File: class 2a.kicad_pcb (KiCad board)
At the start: 2 copper layers, 51.3 x 47.5 mm, 36 parts, among them J1 USB_C_Receptacle, J2 Conn_01x02_Pin, J3 Conn_ARM_JTAG_SWD_10, SW1 SW_SPST, U1 STM32G030F6P6, U2 LR4054, U3 TPS613222ADBV, U4 AMS1117-3.3

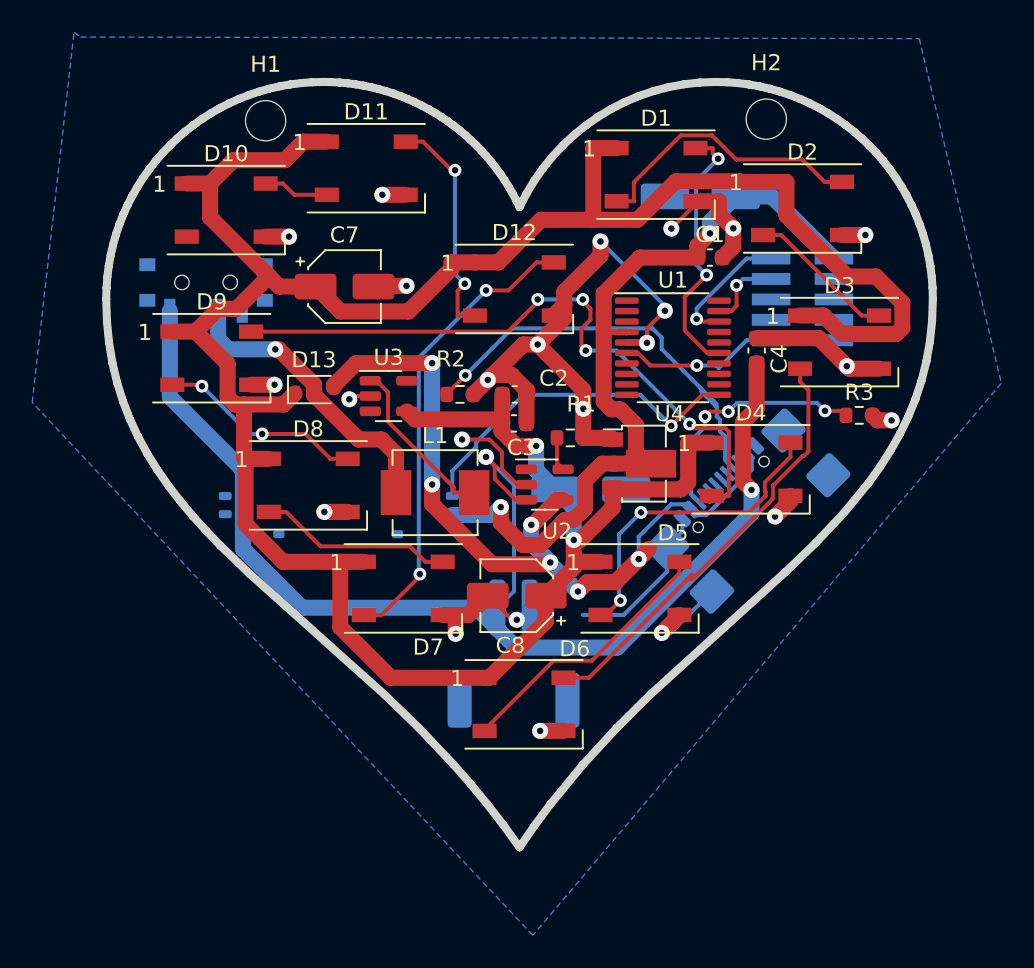
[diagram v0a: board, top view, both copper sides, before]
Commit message: fix resistors for usb-c
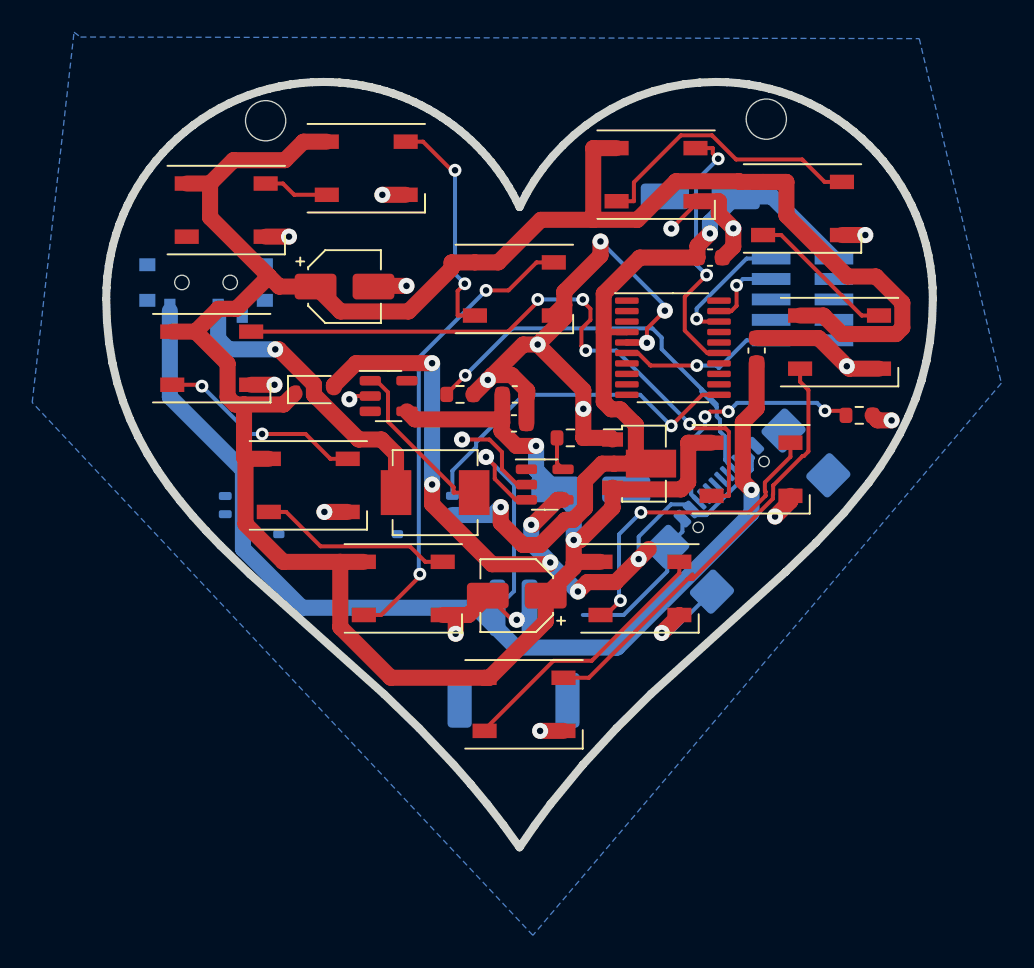
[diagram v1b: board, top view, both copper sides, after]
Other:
- board text removed: "+"
- board text removed: "PCB3D_BR_Heart"
- board text removed: "PCB3D_TL_Heart"

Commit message: rearrange things and use CR2032LIR
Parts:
- removed J2: Conn_01x02_Pin, Connector_JST:JST_PH_S2B-PH-SM4-TB_1x02-1MP_P2.00mm_Horizontal
- added BT1: CS2032-LIR rechargeable, Battery:BatteryHolder_Keystone_1060_1x2032, B.Cu at (135.7, 81.6)
- moved SW1 24.9 mm to (151.7, 69.1), turned to 50 degrees
- moved RV1 23.9 mm to (162.1, 88.9), turned to 47 degrees
- moved J1 15.7 mm to (150.1, 99.9), turned to -133 degrees
- moved C6 10.3 mm to (156.0, 79.4)
- moved C5 5.00 mm to (156.2, 86.1), turned to 180 degrees
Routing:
- net +5V: track 172.3 -> 0.00 mm, vias 2 -> 0
- net GND: track 98.8 -> 0.00 mm, vias 23 -> 0
- net /VBat: track 80.0 -> 0.00 mm, vias 2 -> 0
- net /VUSB: track 49.9 -> 0.00 mm, vias 6 -> 0
- net +3V3: track 48.4 -> 0.00 mm, vias 2 -> 0
- net Net-(D4-DOUT): track 41.3 -> 0.00 mm, vias 4 -> 0
- net Net-(D12-DIN): track 28.9 -> 0.00 mm, vias 2 -> 0
- net Net-(D3-DOUT): track 27.3 -> 0.00 mm
- net Net-(J1-CC1): track 26.6 -> 0.00 mm, vias 1 -> 0
- net /brightness: track 21.8 -> 0.00 mm, vias 1 -> 0
- net Net-(D4-DIN): track 19.8 -> 0.00 mm, vias 2 -> 0
- net /VBat_switched: track 18.5 -> 0.00 mm, vias 1 -> 0
- net Net-(D1-DOUT): track 17.6 -> 0.00 mm
- net Net-(D5-DIN): track 16.9 -> 0.00 mm
- net /LED_Data: track 16.7 -> 0.00 mm, vias 2 -> 0
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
